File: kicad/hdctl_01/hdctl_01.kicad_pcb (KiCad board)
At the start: 4 copper layers, 99.1 x 56.1 mm, 15 parts, among them J1 DIN41612_02x32_AC, J2 Conn_02x20_Odd_Even, SW1 SW_DIP_x04, U1 PAL20RS10, U2 74HCT574, U3 74HCT574, U4 74HC245, U5 74HC193

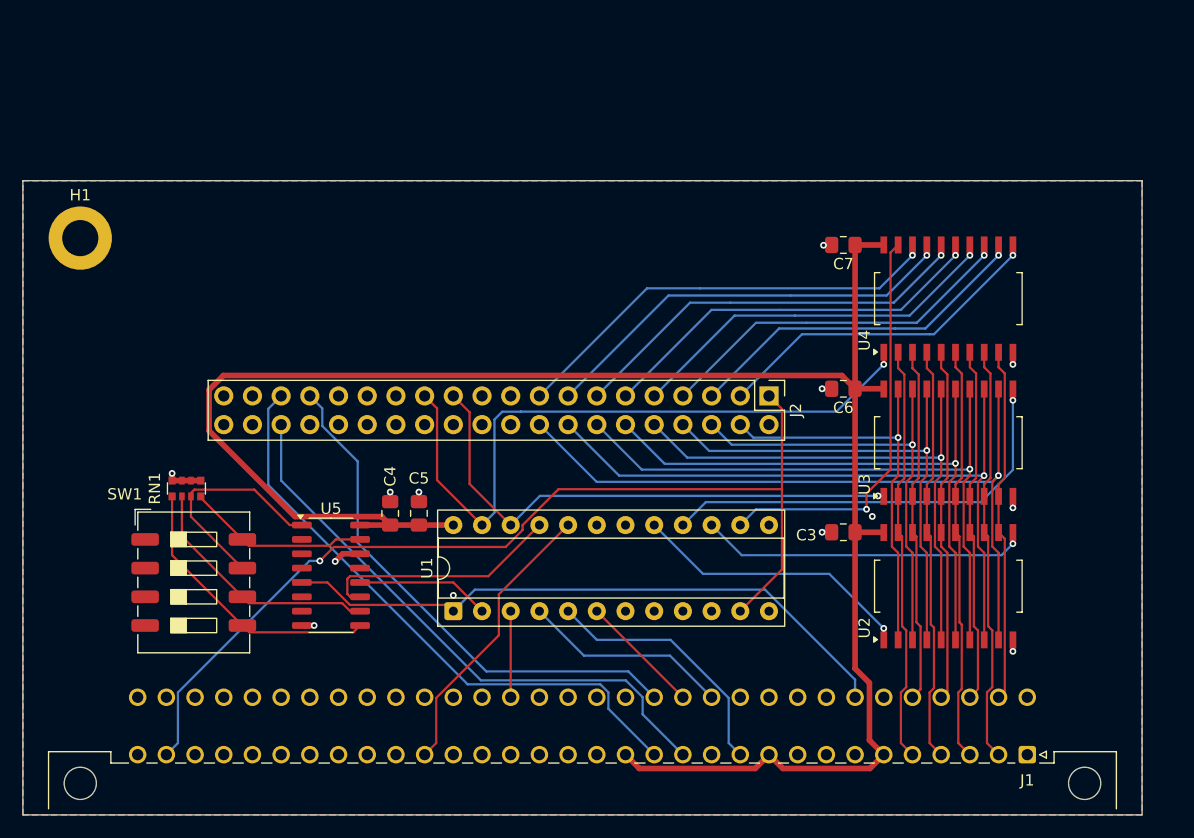
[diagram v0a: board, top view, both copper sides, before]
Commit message: hd controller rework. should be ready for mfg (need final check)
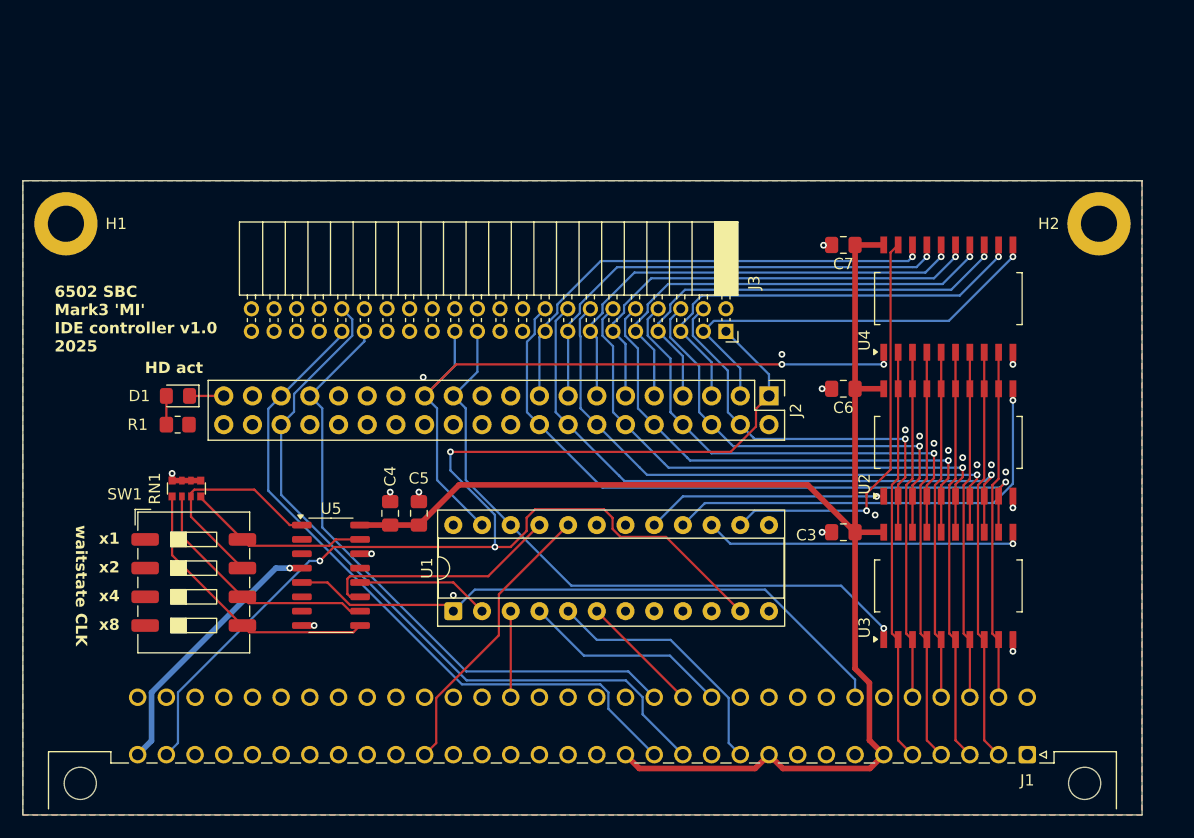
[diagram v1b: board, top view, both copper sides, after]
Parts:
- added D1: LED, LED_SMD:LED_0805_2012Metric_Pad1.15x1.40mm_HandSolder, F.Cu at (54.4, 105.4)
- added H2: GND, MountingHole:MountingHole_3.2mm_M3_DIN965_Pad, F.Cu at (135.9, 90.2)
- added J3: Conn_02x22_Odd_Even, Connector_PinSocket_2.00mm:PinSocket_2x22_P2.00mm_Horizontal, F.Cu at (102.9, 99.7)
- added R1: R, Resistor_SMD:R_0805_2012Metric_Pad1.20x1.40mm_HandSolder, F.Cu at (54.3, 108.0)
- moved U2 12.7 mm to (122.6, 109.5)
- moved U3 12.7 mm to (122.6, 122.2)
- moved H1 1.80 mm to (44.5, 90.2)
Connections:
- J1 pad a1: unconnected-(J1-Pin_a1-Pada1) -> VCC
- J1 pad a20: unconnected-(J1-Pin_a20-Pada20) -> VCC
- J1 pad a32: unconnected-(J1-Pin_a32-Pada32) -> VCC
- J2 pad 39: unconnected-(J2-Pin_39-Pad39) -> Net-(D1-K)
- J2 pad 40: unconnected-(J2-Pin_40-Pad40) -> GND
- U1 pad 15: /~{LATCH_HI} -> /~{LATCH_HI_WR}
- U1 pad 16: /~{LATCH_HI_WR} -> /~{LATCH_HI}
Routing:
- net /~{RES}: track 88.2 -> 115.9 mm, vias 1 -> 3
- net VCC: track 168.3 -> 149.6 mm, vias 0 -> 1
- net /AB2: track 51.5 -> 65.4 mm
- net /~{HD_WR}: track 47.6 -> 57.9 mm
- net /~{LATCH_HI_WR}: track 38.4 -> 28.4 mm
- net /~{LATCH_HI}: track 29.2 -> 39.1 mm
- net /AB1: track 46.7 -> 55.4 mm
- net /AB0: track 53.3 -> 61.5 mm
- net /HD06: track 31.5 -> 39.5 mm
- net /HD07: track 30.2 -> 38.2 mm
- net /HD04: track 33.1 -> 40.5 mm
- net /HD05: track 32.7 -> 39.0 mm
- net /HD03: track 35.3 -> 41.0 mm
- net /HD15: track 65.6 -> 59.9 mm
- net /HD13: track 57.3 -> 52.1 mm
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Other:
- board text added: "6502 SBC Mark3 'MI' IDE controller v1.0 2025"
- board text added: "HD act"
- board text added: "waitstate CLK"
- board text added: "x1"
- board text added: "x2"
- board text added: "x4"
- board text added: "x8"

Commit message: added port on the side
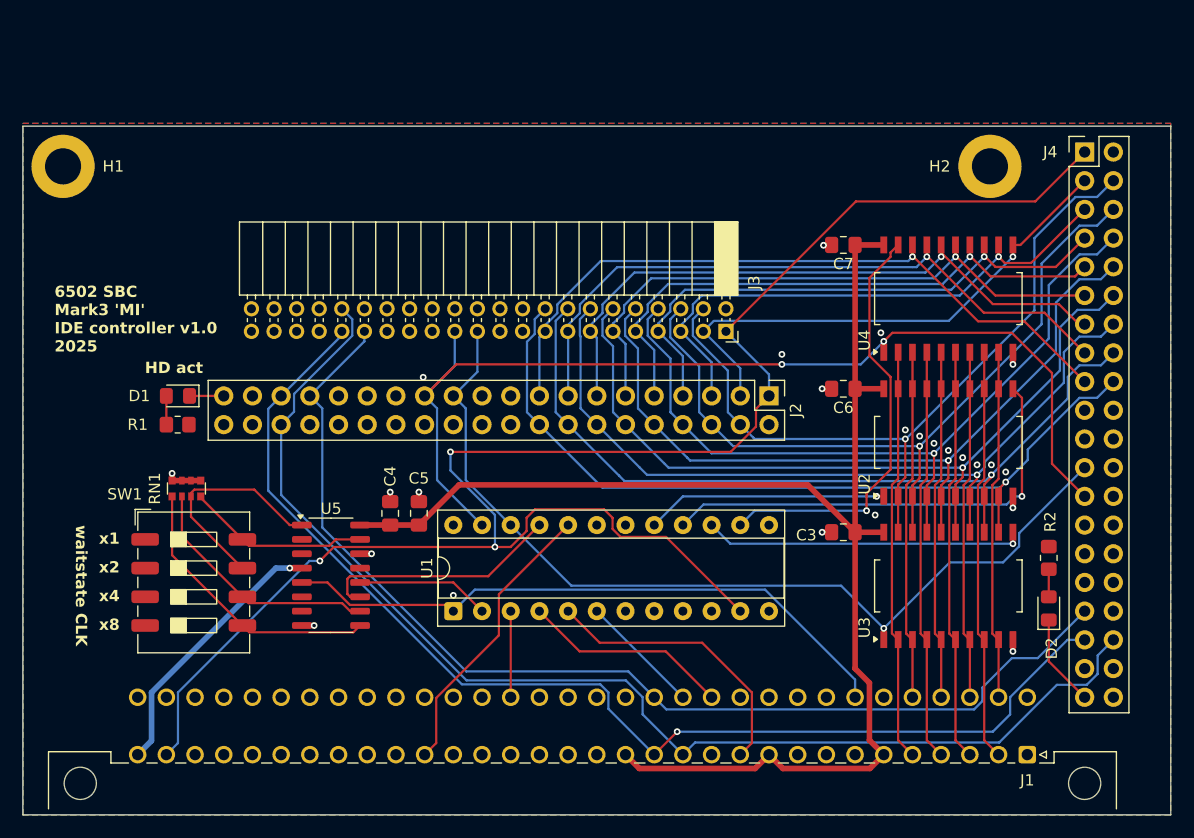
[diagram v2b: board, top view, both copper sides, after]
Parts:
- added D2: LED, LED_SMD:LED_0805_2012Metric_Pad1.15x1.40mm_HandSolder, F.Cu at (131.4, 124.2)
- added J4: Conn_02x20_Odd_Even, Connector_PinHeader_2.54mm:PinHeader_2x20_P2.54mm_Vertical, F.Cu at (134.6, 83.8)
- added R2: R, Resistor_SMD:R_0805_2012Metric_Pad1.20x1.40mm_HandSolder, F.Cu at (131.4, 119.7)
- moved H2 10.9 mm to (126.2, 85.1)
- moved H1 5.09 mm to (44.2, 85.1)
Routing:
- net /AB2: track 65.4 -> 108.7 mm
- net /AB0: track 61.5 -> 104.7 mm, vias 0 -> 1
- net /AB1: track 55.4 -> 98.3 mm
- net /~{RES}: track 115.9 -> 154.2 mm
- net /HD08: track 36.0 -> 67.7 mm
- net /~{HD_RD}: track 63.2 -> 92.8 mm
- net /HD09: track 39.2 -> 68.2 mm
- net /HD10: track 42.5 -> 69.0 mm
- net /~{HD_WR}: track 57.9 -> 82.3 mm
- net /HD11: track 45.7 -> 70.0 mm
- net /HD12: track 48.9 -> 70.8 mm
- net /HD00: track 43.0 -> 63.8 mm
- net /HD13: track 52.1 -> 71.5 mm
- net /HD01: track 42.1 -> 60.5 mm
- net /HD14: track 56.3 -> 72.6 mm
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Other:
- board size 99.1 x 56.1 mm -> 101.6 x 61 mm

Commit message: routing tweaks
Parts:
- moved D2 0.97 mm to (131.1, 123.3)
- moved R2 0.97 mm to (131.1, 118.9)
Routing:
- net /AB1: track 98.3 -> 101.3 mm
- net /AB2: track 108.7 -> 110.2 mm
- net /AB0: track 104.7 -> 106.0 mm
- net /HD07: track 47.0 -> 48.1 mm
- net Net-(D2-K): track 8.18 -> 9.23 mm
- net /HD02: track 57.5 -> 56.7 mm
- net /HD10: track 69.0 -> 69.8 mm
- net /HD09: track 68.2 -> 68.9 mm
- net /HD15: track 73.6 -> 74.1 mm
- net GND: vias 24 -> 25
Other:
- board text added: "on"

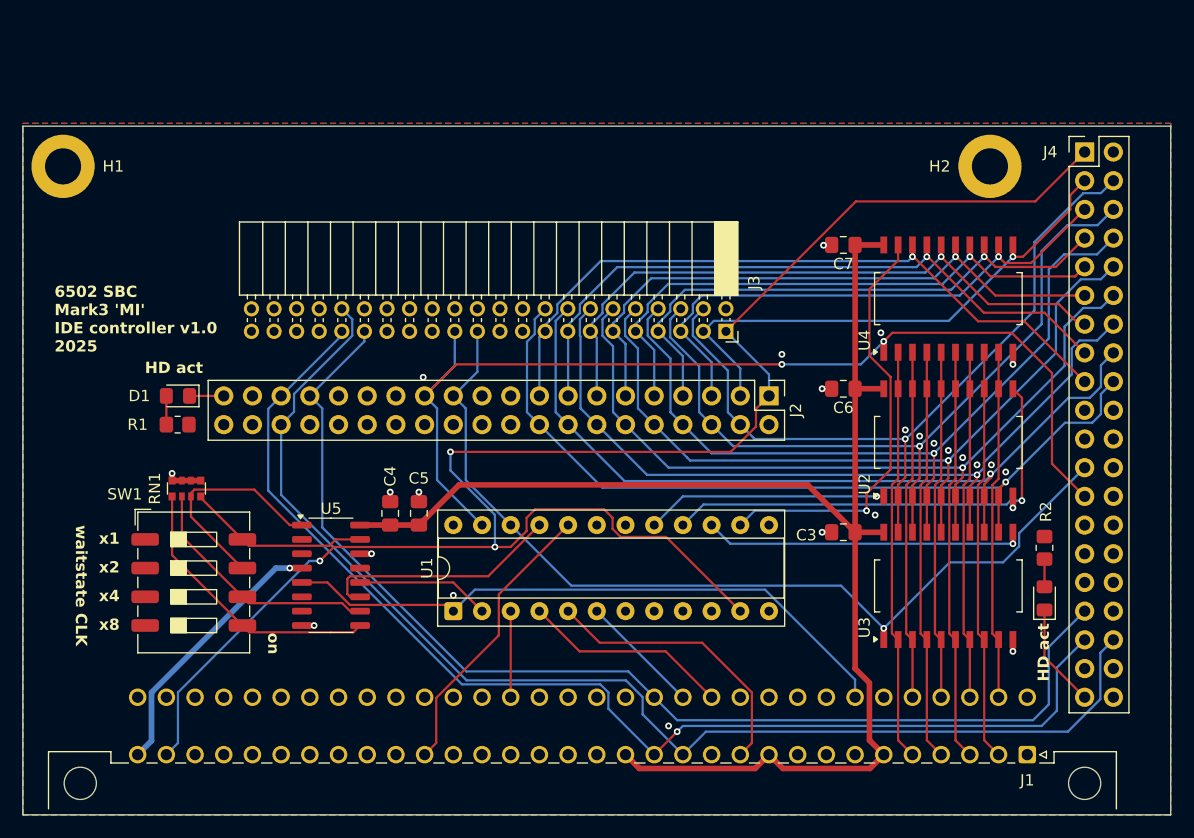
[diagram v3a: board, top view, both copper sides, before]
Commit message: hdctl: update PLD pinout to pcb layout, add monting holes to pcb
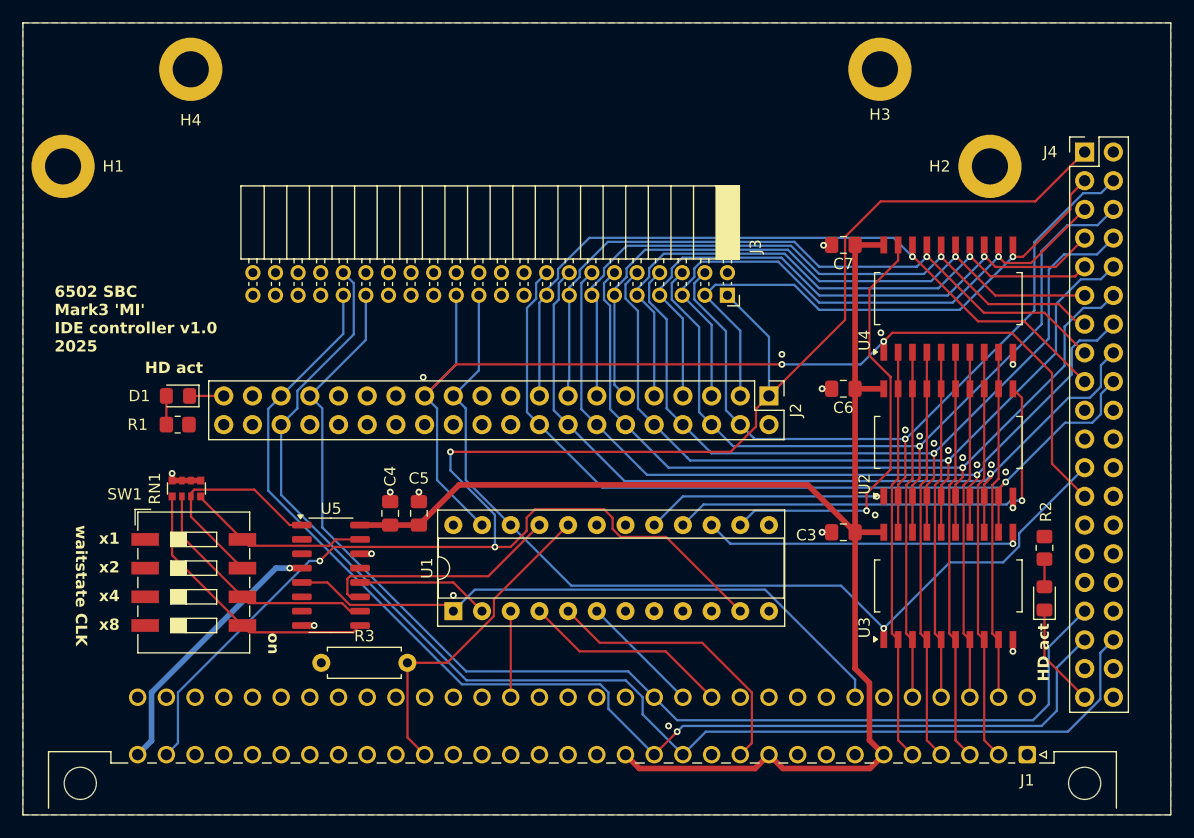
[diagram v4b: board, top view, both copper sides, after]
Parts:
- added H3: GND, MountingHole:MountingHole_3.2mm_M3_DIN965_Pad, F.Cu at (116.5, 76.5)
- added H4: GND, MountingHole:MountingHole_3.2mm_M3_DIN965_Pad, F.Cu at (55.5, 76.5)
- added R3: R, Resistor_THT:R_Axial_DIN0207_L6.3mm_D2.5mm_P7.62mm_Horizontal, F.Cu at (67.1, 129.0)
- moved J3 3.20 mm to (103.0, 96.5)
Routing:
- net /~{RES}: track 154.2 -> 160.2 mm
- net /HD06: track 49.3 -> 54.0 mm
- net /HD05: track 50.3 -> 54.9 mm
- net /HD04: track 52.8 -> 57.0 mm
- net /HD03: track 54.9 -> 58.9 mm
- net /HD02: track 56.7 -> 60.5 mm
- net /HD01: track 60.5 -> 64.1 mm
- net /HD07: track 48.1 -> 51.7 mm
- net /HD14: track 72.9 -> 76.3 mm
- net /RDY: track 25.6 -> 28.9 mm
- net /~{HD_RD}: track 92.8 -> 96.0 mm
- net /HD15: track 74.1 -> 77.4 mm
- net /AB1: track 101.3 -> 104.6 mm
- net /AB0: track 106.0 -> 109.3 mm
- net /~{HD_WR}: track 82.3 -> 85.5 mm
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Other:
- board size 101.6 x 61 mm -> 101.6 x 70.1 mm

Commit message: final (?) hdctl pcb layout
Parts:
- added J5: Conn_01x02_Socket, Connector_PinSocket_2.54mm:PinSocket_1x02_P2.54mm_Vertical, F.Cu at (52.6, 98.5)
- added JP1: SolderJumper_3_Open, Jumper:SolderJumper-3_P1.3mm_Open_RoundedPad1.0x1.5mm, F.Cu at (61.0, 99.7)
- J2, J4: footprint Connector_PinHeader_2.54mm:PinHeader_2x20_P2.54mm_Vertical -> Connector_IDC:IDC-Header_2x20_P2.54mm_Vertical
- moved D1 4.32 mm to (50.0, 105.4)
- moved R1 4.32 mm to (50.0, 108.0)
- moved J4 2.90 mm to (135.8, 81.2)
- moved C6 1.56 mm to (114.3, 105.9), turned to -90 degrees
- moved D2 0.40 mm to (130.7, 123.5)
- moved R2 0.40 mm to (130.7, 119.0)
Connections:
- J2 pad 19: unconnected-(J2-Pin_19-Pad19) -> GND
- J2 pad 22: unconnected-(J2-Pin_22-Pad22) -> GND
- J2 pad 24: unconnected-(J2-Pin_24-Pad24) -> GND
- J2 pad 26: unconnected-(J2-Pin_26-Pad26) -> GND
- J2 pad 30: unconnected-(J2-Pin_30-Pad30) -> GND
- J3 pad 19: unconnected-(J3-Pin_19-Pad19) -> GND
- J3 pad 22: unconnected-(J3-Pin_22-Pad22) -> GND
- J3 pad 24: unconnected-(J3-Pin_24-Pad24) -> GND
- J3 pad 26: unconnected-(J3-Pin_26-Pad26) -> GND
- J3 pad 30: unconnected-(J3-Pin_30-Pad30) -> GND
- J3 pad 40: unconnected-(J3-Pin_40-Pad40) -> GND
- J3 pad 41: unconnected-(J3-Pin_41-Pad41) -> VCC
- J3 pad 42: unconnected-(J3-Pin_42-Pad42) -> /VCC_MOT
- J3 pad 43: unconnected-(J3-Pin_43-Pad43) -> GND
- J4 pad 19: unconnected-(J4-Pin_19-Pad19) -> GND
- J4 pad 22: unconnected-(J4-Pin_22-Pad22) -> GND
- J4 pad 24: unconnected-(J4-Pin_24-Pad24) -> GND
- J4 pad 26: unconnected-(J4-Pin_26-Pad26) -> GND
- J4 pad 30: unconnected-(J4-Pin_30-Pad30) -> GND
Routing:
- net /VCC_MOT: track 0.00 -> 10.0 mm
- net Net-(J5-Pin_2): track 0.00 -> 5.01 mm
- net Net-(D1-K): track 3.03 -> 7.35 mm
- net /HD13: track 74.5 -> 77.7 mm
- net /HD12: track 73.7 -> 76.9 mm
- net /AB0: track 109.3 -> 112.4 mm
- net /~{HD_WR}: track 85.5 -> 88.7 mm
- net /HD08: track 70.6 -> 73.7 mm
- net /AB2: track 113.4 -> 116.5 mm
- net /AB1: track 104.6 -> 107.7 mm
- net /HD11: track 73.1 -> 76.1 mm
- net /HD07: track 51.7 -> 54.4 mm
- net /HD09: track 72.0 -> 74.5 mm
- net /HD14: track 76.3 -> 78.7 mm
- net /HD10: track 72.9 -> 75.3 mm
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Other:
- board text added: "MOT +5"
